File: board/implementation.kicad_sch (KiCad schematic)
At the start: 29 parts, among them Q1 Q_PMOS_DGS, Q2 Q_NMOS_DGS, U1 ALED7709ATR

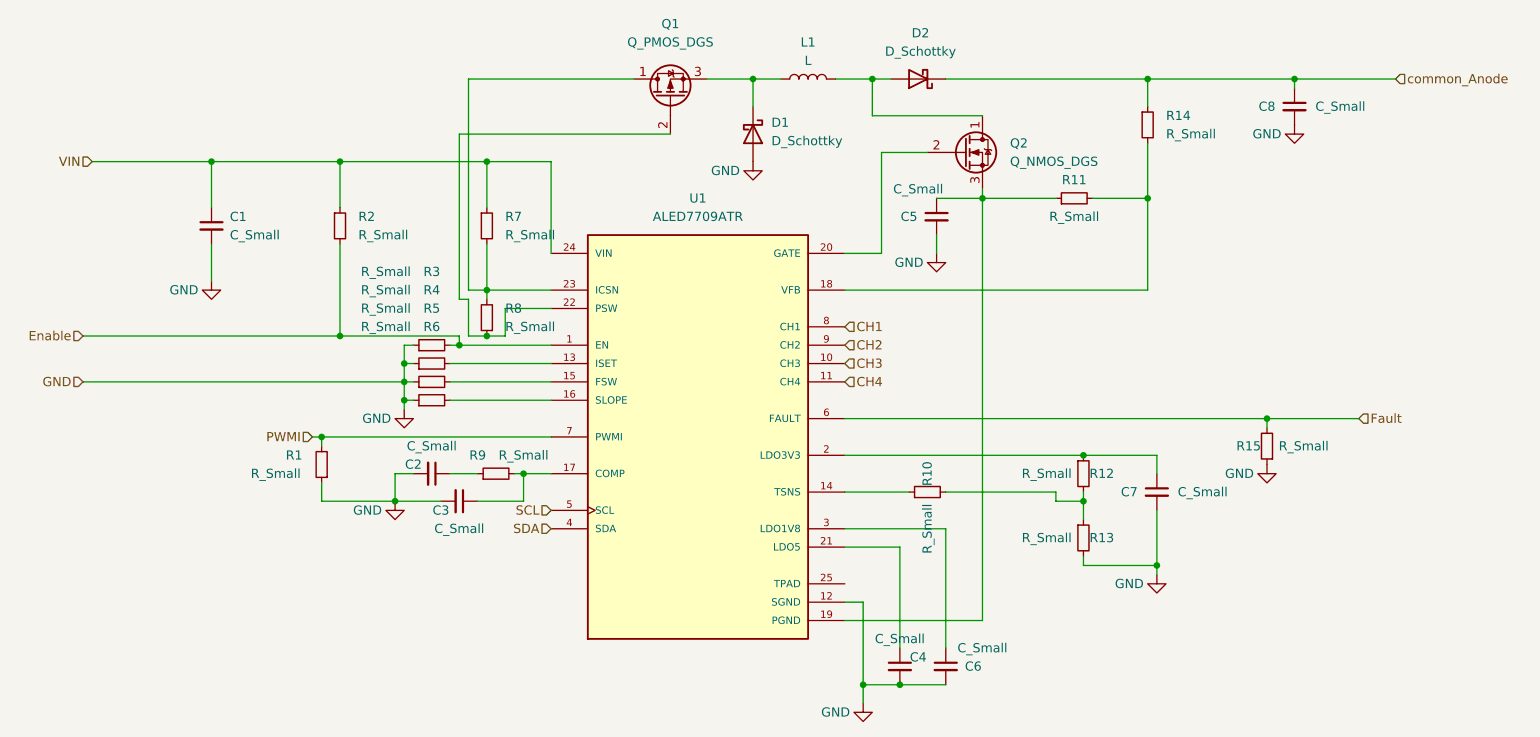
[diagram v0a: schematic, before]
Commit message: Add Testpoint | Add relative footrpint/symbol path
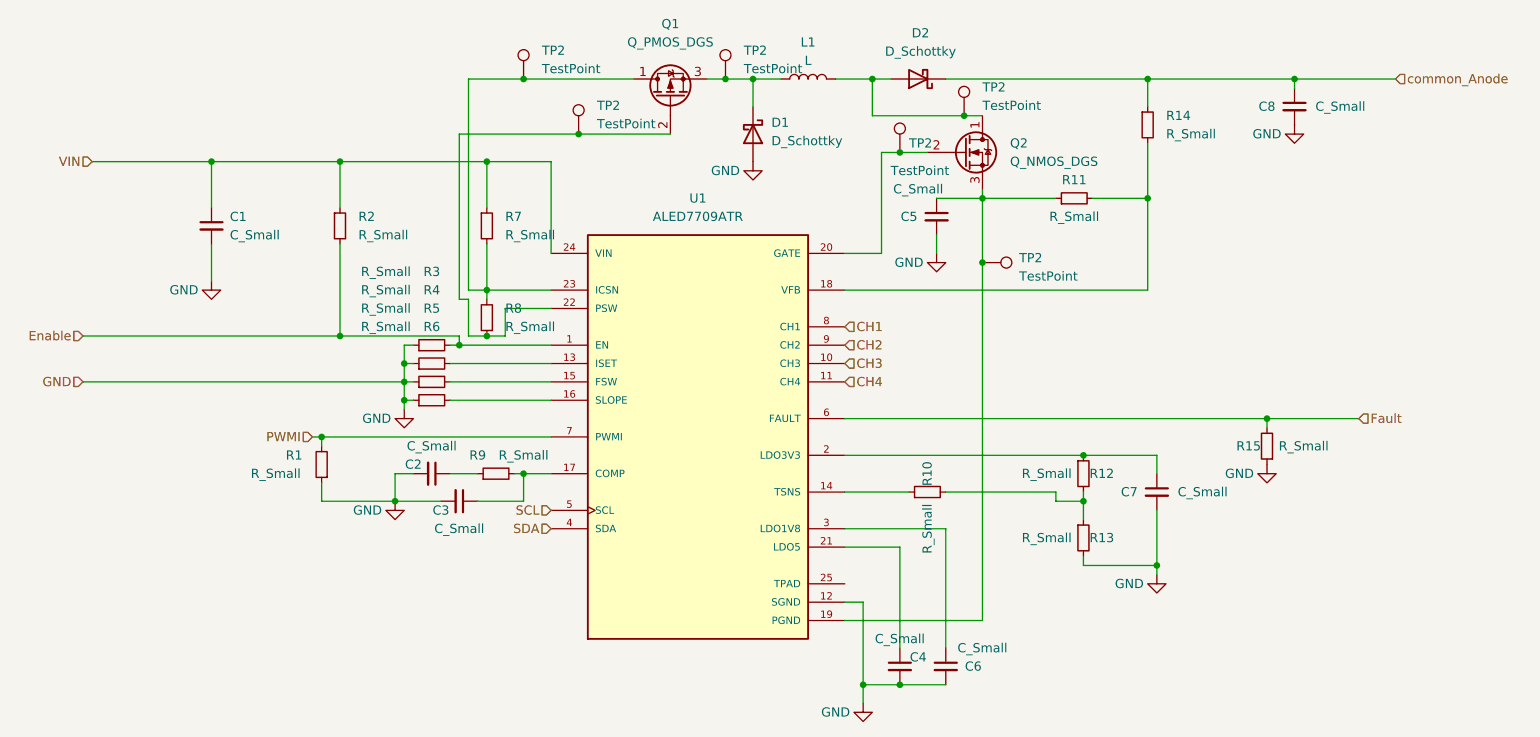
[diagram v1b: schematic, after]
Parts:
- added TP2 (x6): TestPoint, TestPoint:TestPoint_Pad_D1.0mm, symbol Connector:TestPoint
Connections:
- net at C5.1, Q2.3 (S), R11.1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: now also TP2.1
- net at D2.2 (A), L1.2, Q2.1 (D): now also TP2.1
- net at Q2.2 (G), U1.20 (GATE): now also TP2.1
- net at Q1.2 (G), R8.1, U1.22 (PSW): now also TP2.1
- net at Q1.1 (D), R7.2, R8.2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: now also TP2.1
- net at D1.1 (K), L1.1, Q1.3 (S): now also TP2.1
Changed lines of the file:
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@@
   (junction (at 121.92 52.07) (diameter 0) (color 0 0 0 0)
   )
+  (junction (at 190.5 66.04) (diameter 0) (color 0 0 0 0)
+  )
   (junction (at 214.63 107.95) (diameter 0) (color 0 0 0 0)
   )
@@
   (junction (at 110.49 82.55) (diameter 0) (color 0 0 0 0)
   )
+  (junction (at 127 40.64) (diameter 0) (color 0 0 0 0)
+  )
   (junction (at 110.49 80.01) (diameter 0) (color 0 0 0 0)
   )
@@
   (junction (at 83.82 52.07) (diameter 0) (color 0 0 0 0)
   )
+  (junction (at 154.94 40.64) (diameter 0) (color 0 0 0 0)
+  )
   (junction (at 179.07 124.46) (diameter 0) (color 0 0 0 0)
   )
@@
   (junction (at 173.99 124.46) (diameter 0) (color 0 0 0 0)
   )
+  (junction (at 179.07 50.8) (diameter 0) (color 0 0 0 0)
+  )
   (junction (at 121.92 69.85) (diameter 0) (color 0 0 0 0)
   )
@@
   (junction (at 109.22 99.06) (diameter 0) (color 0 0 0 0)
   )
+  (junction (at 134.62 48.26) (diameter 0) (color 0 0 0 0)
+  )
+  (junction (at 187.96 45.72) (diameter 0) (color 0 0 0 0)
+  )
   (junction (at 127 95.25) (diameter 0) (color 0 0 0 0)
   )
@@
     (stroke (width 0) (type default))
   )
-  (wire (pts (xy 182.88 50.8) (xy 176.53 50.8))
+  (wire (pts (xy 182.88 50.8) (xy 179.07 50.8))
     (stroke (width 0) (type default))
   )
@@
     (stroke (width 0) (type default))
   )
+  (wire (pts (xy 154.94 40.64) (xy 152.4 40.64))
+    (stroke (width 0) (type default))
+  )
   (wire (pts (xy 214.63 109.22) (xy 214.63 107.95))
     (stroke (width 0) (type default))
   )
+  (wire (pts (xy 190.5 66.04) (xy 190.5 57.15))
+    (stroke (width 0) (type default))
+  )
   (wire (pts (xy 120.65 99.06) (xy 127 99.06))
     (stroke (width 0) (type default))
@@
     (stroke (width 0) (type default))
   )
-  (wire (pts (xy 118.11 48.26) (xy 147.32 48.26))
+  (wire (pts (xy 118.11 48.26) (xy 134.62 48.26))
     (stroke (width 0) (type default))
   )
@@
     (stroke (width 0) (type default))
   )
-  (wire (pts (xy 190.5 115.57) (xy 190.5 57.15))
+  (wire (pts (xy 190.5 115.57) (xy 190.5 66.04))
     (stroke (width 0) (type default))
   )
@@
     (stroke (width 0) (type default))
   )
+  (wire (pts (xy 134.62 48.26) (xy 147.32 48.26))
+    (stroke (width 0) (type default))
+  )
+  (wire (pts (xy 127 40.64) (xy 142.24 40.64))
+    (stroke (width 0) (type default))
+  )
   (wire (pts (xy 204.47 97.79) (xy 204.47 99.06))
     (stroke (width 0) (type default))
   )
+  (wire (pts (xy 187.96 45.72) (xy 190.5 45.72))
+    (stroke (width 0) (type default))
+  )
   (wire (pts (xy 171.45 113.03) (xy 173.99 113.03))
     (stroke (width 0) (type default))
@@
     (stroke (width 0) (type default))
   )
-  (wire (pts (xy 158.75 40.64) (xy 152.4 40.64))
+  (wire (pts (xy 158.75 40.64) (xy 154.94 40.64))
     (stroke (width 0) (type default))
   )
@@
     (stroke (width 0) (type default))
   )
+  (wire (pts (xy 179.07 50.8) (xy 176.53 50.8))
+    (stroke (width 0) (type default))
+  )
   (wire (pts (xy 171.45 105.41) (xy 179.07 105.41))
     (stroke (width 0) (type default))
@@
     (stroke (width 0) (type default))
   )
-  (wire (pts (xy 175.26 45.72) (xy 190.5 45.72))
+  (wire (pts (xy 175.26 45.72) (xy 187.96 45.72))
     (stroke (width 0) (type default))
   )
@@
     (stroke (width 0) (type default))
   )
-  (wire (pts (xy 119.38 40.64) (xy 142.24 40.64))
+  (wire (pts (xy 119.38 40.64) (xy 127 40.64))
     (stroke (width 0) (type default))
   )
@@
     )
   )
+  (symbol (lib_id "Connector:TestPoint") (at 134.62 48.26 0) (unit 1)
+    (in_bom yes) (on_board yes) (dnp no) (fields_autoplaced)
+    (property "Reference" "TP2" (at 137.16 44.323 0)
+      (effects (font (size 1.27 1.27)) (justify left))
+    )
+    (property "Value" "TestPoint" (at 137.16 46.863 0)
+      (effects (font (size 1.27 1.27)) (justify left))
+    )
+    (property "Footprint" "TestPoint:TestPoint_Pad_D1.0mm" (at 139.7 48.26 0)
+      (effects (font (size 1.27 1.27)) hide)
+    )
+    (property "Datasheet" "~" (at 139.7 48.26 0)
+      (effects (font (size 1.27 1.27)) hide)
+    )
+    (pin "1")
+    (instances
+      (project "board"
+        (path "/57732dd3-1162-4c3f-88bd-31bf473d124d"
+          (reference "TP2") (unit 1)
+        )
+        (path "/57732dd3-1162-4c3f-88bd-31bf473d124d/767ce4c6-0e55-4543-92f0-34cb8237a544"
+          (reference "TP6") (unit 1)
+        )
+      )
+    )
+  )
   (symbol (lib_id "Device:R_Small") (at 114.3 82.55 90) (unit 1)
     (in_bom yes) (on_board yes) (dnp no)
@@
     )
   )
+  (symbol (lib_id "Connector:TestPoint") (at 190.5 66.04 270) (unit 1)
+    (in_bom yes) (on_board yes) (dnp no) (fields_autoplaced)
+    (property "Reference" "TP2" (at 195.58 65.405 90)
+      (effects (font (size 1.27 1.27)) (justify left))
+    )
+    (property "Value" "TestPoint" (at 195.58 67.945 90)
+      (effects (font (size 1.27 1.27)) (justify left))
+    )
+    (property "Footprint" "TestPoint:TestPoint_Pad_D1.0mm" (at 190.5 71.12 0)
+      (effects (font (size 1.27 1.27)) hide)
+    )
+    (property "Datasheet" "~" (at 190.5 71.12 0)
+      (effects (font (size 1.27 1.27)) hide)
+    )
+    (pin "1")
+    (instances
+      (project "board"
+        (path "/57732dd3-1162-4c3f-88bd-31bf473d124d"
+          (reference "TP2") (unit 1)
+        )
+        (path "/57732dd3-1162-4c3f-88bd-31bf473d124d/767ce4c6-0e55-4543-92f0-34cb8237a544"
+          (reference "TP9") (unit 1)
+        )
+      )
+    )
+  )
   (symbol (lib_id "Device:C_Small") (at 118.11 99.06 270) (unit 1)
     (in_bom yes) (on_board yes) (dnp no)
@@
         (path "/57732dd3-1162-4c3f-88bd-31bf473d124d/767ce4c6-0e55-4543-92f0-34cb8237a544"
           (reference "Q2") (unit 1)
+        )
+      )
+    )
+  )
+  (symbol (lib_id "Connector:TestPoint") (at 179.07 50.8 0) (unit 1)
+    (in_bom yes) (on_board yes) (dnp no)
+    (property "Reference" "TP2" (at 180.34 49.53 0)
+      (effects (font (size 1.27 1.27)) (justify left))
+    )
+    (property "Value" "TestPoint" (at 177.8 53.34 0)
+      (effects (font (size 1.27 1.27)) (justify left))
+    )
+    (property "Footprint" "TestPoint:TestPoint_Pad_D1.0mm" (at 184.15 50.8 0)
+      (effects (font (size 1.27 1.27)) hide)
+    )
+    (property "Datasheet" "~" (at 184.15 50.8 0)
+      (effects (font (size 1.27 1.27)) hide)
+    )
+    (pin "1")
+    (instances
+      (project "board"
+        (path "/57732dd3-1162-4c3f-88bd-31bf473d124d"
+          (reference "TP2") (unit 1)
+        )
+        (path "/57732dd3-1162-4c3f-88bd-31bf473d124d/767ce4c6-0e55-4543-92f0-34cb8237a544"
+          (reference "TP7") (unit 1)
         )
       )
@@
     )
   )
+  (symbol (lib_id "Connector:TestPoint") (at 127 40.64 0) (unit 1)
+    (in_bom yes) (on_board yes) (dnp no) (fields_autoplaced)
+    (property "Reference" "TP2" (at 129.54 36.703 0)
+      (effects (font (size 1.27 1.27)) (justify left))
+    )
+    (property "Value" "TestPoint" (at 129.54 39.243 0)
+      (effects (font (size 1.27 1.27)) (justify left))
+    )
+    (property "Footprint" "TestPoint:TestPoint_Pad_D1.0mm" (at 132.08 40.64 0)
+      (effects (font (size 1.27 1.27)) hide)
+    )
+    (property "Datasheet" "~" (at 132.08 40.64 0)
+      (effects (font (size 1.27 1.27)) hide)
+    )
+    (pin "1")
+    (instances
+      (project "board"
+        (path "/57732dd3-1162-4c3f-88bd-31bf473d124d"
+          (reference "TP2") (unit 1)
+        )
+        (path "/57732dd3-1162-4c3f-88bd-31bf473d124d/767ce4c6-0e55-4543-92f0-34cb8237a544"
+          (reference "TP4") (unit 1)
+        )
+      )
+    )
+  )
+  (symbol (lib_id "Connector:TestPoint") (at 187.96 45.72 0) (unit 1)
+    (in_bom yes) (on_board yes) (dnp no) (fields_autoplaced)
+    (property "Reference" "TP2" (at 190.5 41.783 0)
+      (effects (font (size 1.27 1.27)) (justify left))
+    )
+    (property "Value" "TestPoint" (at 190.5 44.323 0)
+      (effects (font (size 1.27 1.27)) (justify left))
+    )
+    (property "Footprint" "TestPoint:TestPoint_Pad_D1.0mm" (at 193.04 45.72 0)
+      (effects (font (size 1.27 1.27)) hide)
+    )
+    (property "Datasheet" "~" (at 193.04 45.72 0)
+      (effects (font (size 1.27 1.27)) hide)
+    )
+    (pin "1")
+    (instances
+      (project "board"
+        (path "/57732dd3-1162-4c3f-88bd-31bf473d124d"
+          (reference "TP2") (unit 1)
+        )
+        (path "/57732dd3-1162-4c3f-88bd-31bf473d124d/767ce4c6-0e55-4543-92f0-34cb8237a544"
+          (reference "TP8") (unit 1)
+        )
+      )
+    )
+  )
   (symbol (lib_id "Device:R_Small") (at 101.6 60.96 0) (unit 1)
     (in_bom yes) (on_board yes) (dnp no) (fields_autoplaced)
@@
         )
       )
+    )
+  )
+  (symbol (lib_id "Connector:TestPoint") (at 154.94 40.64 0) (unit 1)
+    (in_bom yes) (on_board yes) (dnp no) (fields_autoplaced)
+    (property "Reference" "TP2" (at 157.48 36.703 0)
+      (effects (font (size 1.27 1.27)) (justify left))
+    )
+    (property "Value" "TestPoint" (at 157.48 39.243 0)
+      (effects (font (size 1.27 1.27)) (justify left))
+    )
+    (property "Footprint" "TestPoint:TestPoint_Pad_D1.0mm" (at 160.02 40.64 0)
+      (effects (font (size 1.27 1.27)) hide)
+    )
+    (property "Datasheet" "~" (at 160.02 40.64 0)
+      (effects (font (size 1.27 1.27)) hide)
+    )
+    (pin "1")
+    (instances
+      (project "board"
+        (path "/57732dd3-1162-4c3f-88bd-31bf473d124d"
+          (reference "TP2") (unit 1)
+        )
+        (path "/57732dd3-1162-4c3f-88bd-31bf473d124d/767ce4c6-0e55-4543-92f0-34cb8237a544"
+          (reference "TP5") (unit 1)
+        )
+      )
